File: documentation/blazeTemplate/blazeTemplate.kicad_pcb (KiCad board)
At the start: 4 copper layers, 70 x 70 mm, 11 parts, among them J1 FrontInterconnect, J2 RearInterconnect, U1 TCAN1044VDDFR

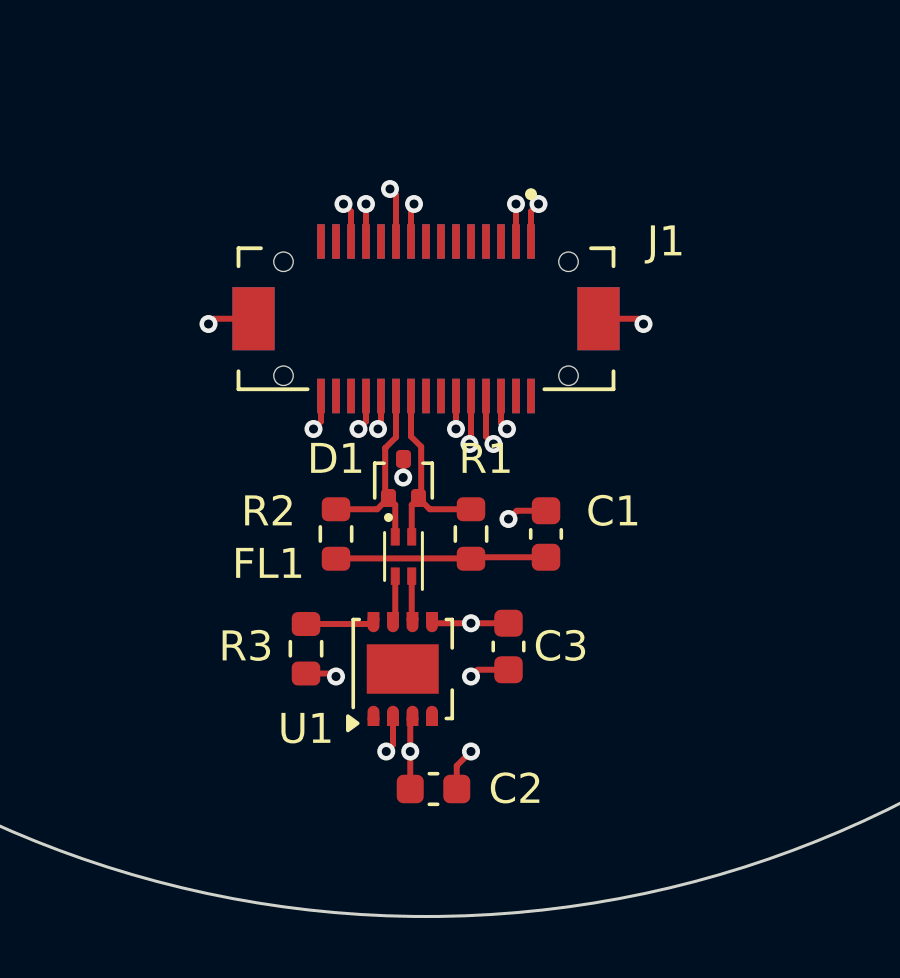
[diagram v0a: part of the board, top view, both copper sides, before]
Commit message: Added 3D models
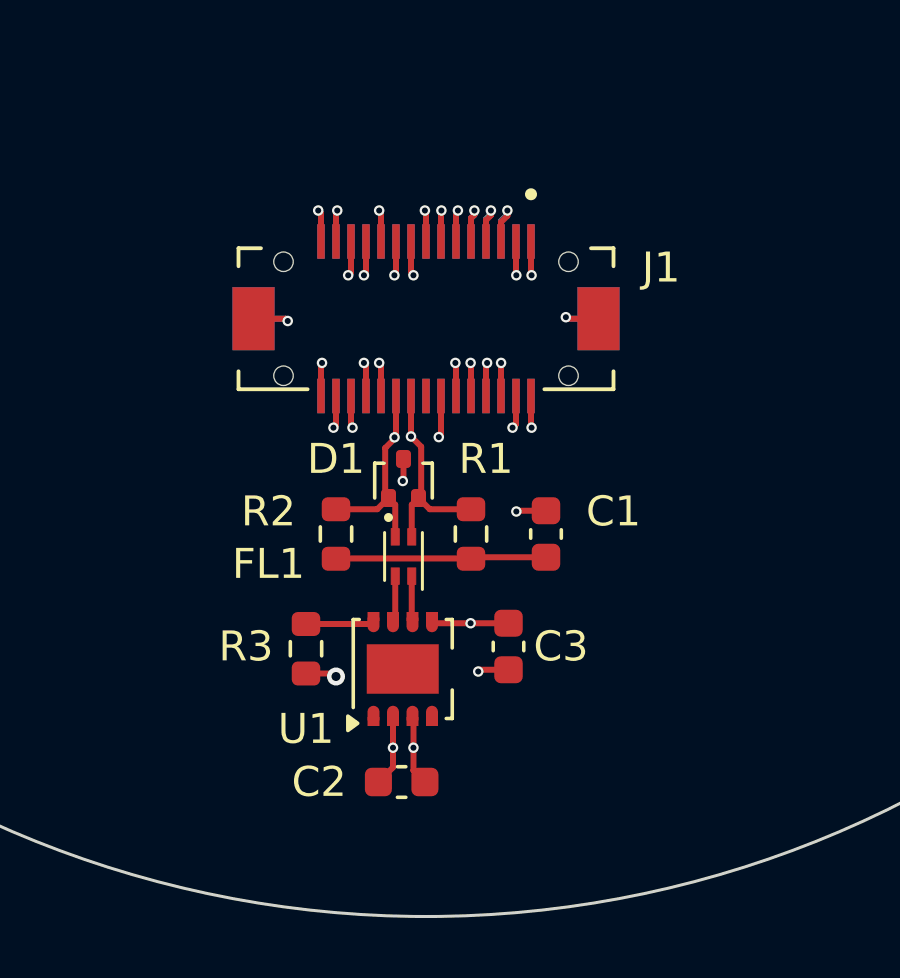
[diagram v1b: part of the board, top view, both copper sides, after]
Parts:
- moved C2 1.09 mm to (147.7, 136.0), turned to 180 degrees
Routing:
- net GND: track 16.8 -> 23.2 mm, vias 13 -> 12
- net +3V3: track 9.52 -> 12.6 mm
- net /TX_RADIO: track 0.00 -> 2.24 mm, vias 0 -> 1
- net Net-(J1-Pin_29): track 0.00 -> 2.21 mm, vias 0 -> 1
- net /RX_RADIO: track 0.00 -> 2.20 mm, vias 0 -> 1
- net Net-(J1-Pin_17): track 0.00 -> 2.18 mm, vias 0 -> 1
- net Net-(J1-Pin_5): track 0.00 -> 2.16 mm, vias 0 -> 1
- net Net-(J1-Pin_18): track 0.00 -> 2.15 mm, vias 0 -> 1
- net Net-(J1-Pin_15): track 0.00 -> 2.14 mm, vias 0 -> 1
- net Net-(J1-Pin_30): track 0.00 -> 2.13 mm, vias 0 -> 1
- net /ARM: track 0.00 -> 2.12 mm, vias 0 -> 1
- net /PPS: track 0.00 -> 2.12 mm, vias 0 -> 1
- net Net-(J1-Pin_14): track 0.00 -> 2.10 mm, vias 0 -> 1
- net Net-(J1-Pin_8): track 0.00 -> 2.10 mm, vias 0 -> 1
- net Net-(J1-Pin_7): track 0.00 -> 2.08 mm, vias 0 -> 1
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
